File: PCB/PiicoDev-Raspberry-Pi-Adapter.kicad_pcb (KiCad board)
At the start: 2 copper layers, 22.1 x 51.6 mm, 12 parts, among them J1 Raspberry_Pi_2_3, J2 Conn_PiicoDev_socket, J3 Conn_PiicoDev_socket, J4 Conn_PiicoDev_socket, J5 Conn_PiicoDev_socket, J6 Prototyping Header

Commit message: Add Logo to silkscreen
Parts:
- added G***: LOGO, CoreElectronics_Artwork:CoreElectronics_logo_5mm_v2, F.Cu at (126.2, 77.3)

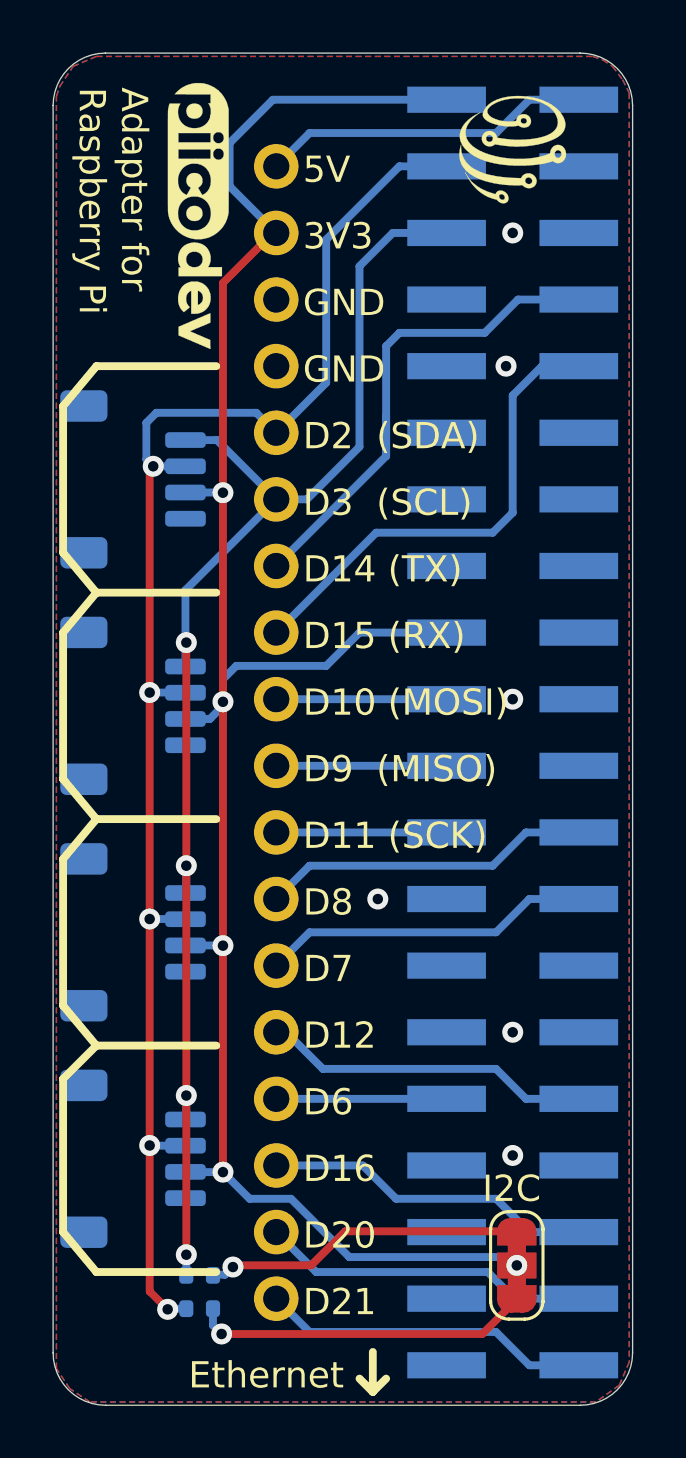
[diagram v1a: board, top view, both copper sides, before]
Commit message: Bump to v11 - update header footprint to include post-holes
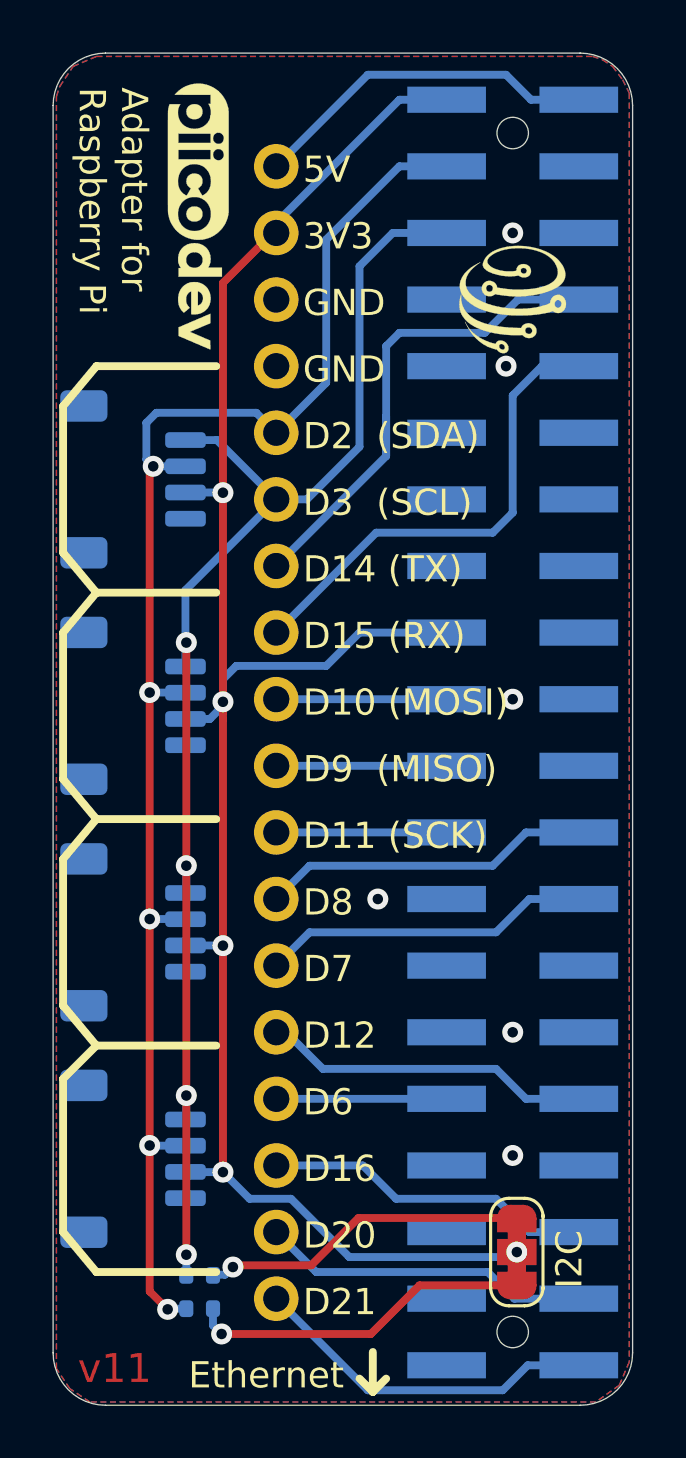
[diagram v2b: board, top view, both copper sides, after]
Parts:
- J1: footprint Connector_PinSocket_2.54mm:PinSocket_2x20_P2.54mm_Vertical_SMD -> CoreElectronics_Components:PinSocket_2x20_P2.54mm_Vertical_SMD_With_Post
- moved G*** 5.72 mm to (126.2, 83.1)
- moved JP1 0.51 mm to (126.4, 119.4)
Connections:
- J1 pad 11: (no net) -> Net-(J1-Pad11)
- J1 pad 12: (no net) -> Net-(J1-Pad12)
- J1 pad 13: (no net) -> Net-(J1-Pad13)
- J1 pad 15: (no net) -> Net-(J1-Pad15)
- J1 pad 16: (no net) -> Net-(J1-Pad16)
- J1 pad 18: (no net) -> Net-(J1-Pad18)
- J1 pad 22: (no net) -> Net-(J1-Pad22)
- J1 pad 27: (no net) -> Net-(J1-Pad27)
- J1 pad 28: (no net) -> Net-(J1-Pad28)
- J1 pad 29: (no net) -> Net-(J1-Pad29)
- J1 pad 33: (no net) -> Net-(J1-Pad33)
- J1 pad 34: GND -> Net-(J1-Pad34)
- J1 pad 35: (no net) -> Net-(J1-Pad35)
- J1 pad 37: (no net) -> Net-(J1-Pad37)
- J1 pad 39: GND -> Net-(J1-Pad39)
- J1 pad 4: (no net) -> Net-(J1-Pad4)
- J1 pad 7: (no net) -> Net-(J1-Pad7)
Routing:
- net +3V3: track 78.7 -> 74.4 mm
- net /D21: track 12.6 -> 13.4 mm
- net +5V: track 12.6 -> 13.4 mm
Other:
- board text added: "v11"

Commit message: Add 120R to SCL & SDA.  Improve silk screen.
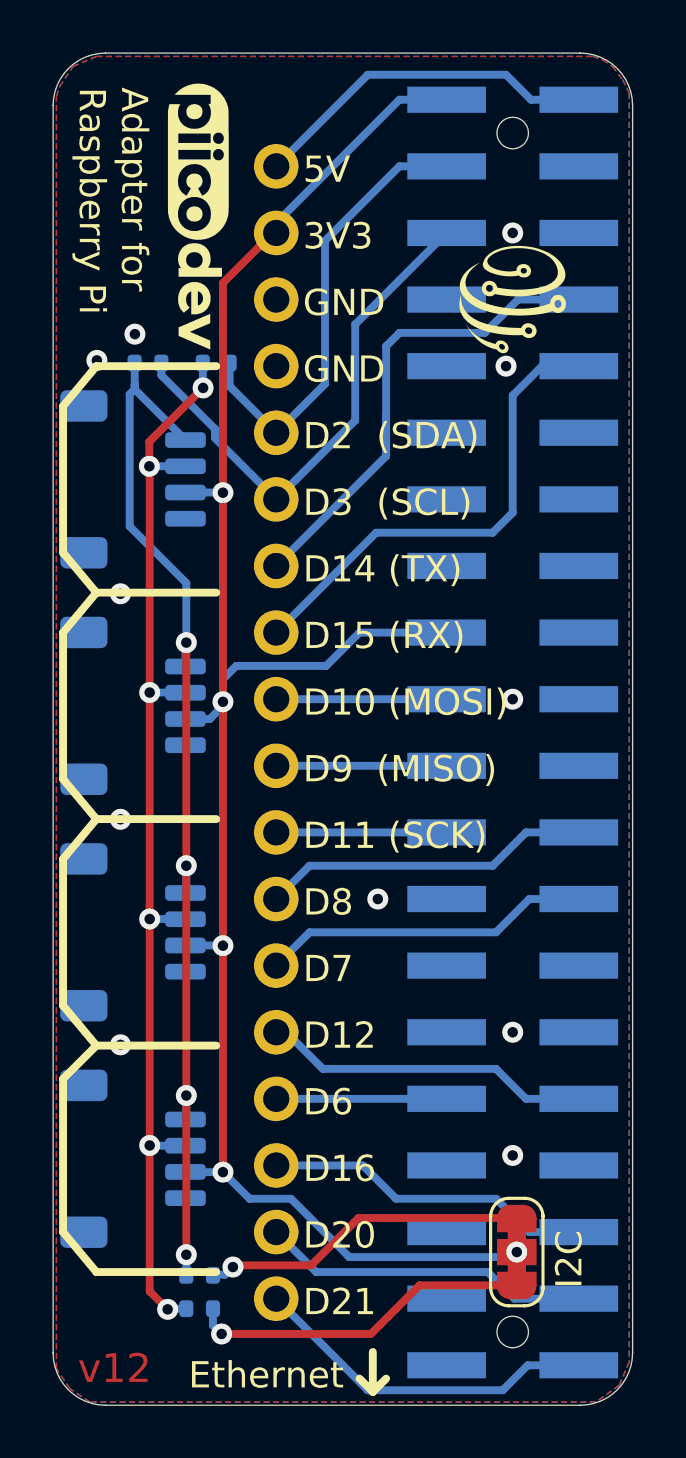
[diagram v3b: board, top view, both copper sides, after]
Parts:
- added R3: 120R, Resistor_SMD:R_0402_1005Metric, B.Cu at (114.9, 85.5)
- added R4: 120R, Resistor_SMD:R_0402_1005Metric, B.Cu at (112.3, 85.5)
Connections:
- J2 pad 3: /SDA -> /SDA_R
- J2 pad 4: /SCL -> /SCL_R
- J3 pad 3: /SDA -> /SDA_R
- J3 pad 4: /SCL -> /SCL_R
- J4 pad 3: /SDA -> /SDA_R
- J4 pad 4: /SCL -> /SCL_R
- J5 pad 1: GND -> Net-(J5-Pad1)
- J5 pad 3: /SDA -> /SDA_R
- J5 pad 4: /SCL -> /SCL_R
- R1 pad 2: /SDA -> /SDA_R
- R2 pad 2: /SCL -> /SCL_R
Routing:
- net /SDA_R: track 0.00 -> 43.7 mm, vias 0 -> 6
- net /SDA: track 59.6 -> 17.3 mm, vias 5 -> 0
- net /SCL_R: track 0.00 -> 41.6 mm, vias 0 -> 4
- net /SCL: track 53.1 -> 22.0 mm, vias 4 -> 0
- net GND: vias 6 -> 11
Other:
- board text added: "v12"
- board text removed: "v11"

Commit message: v13
Add Raspberry Pi connector pin numbers to silk screen
Update solder jumper with thinner cut trace
Fix PiicoDev connector ground connection
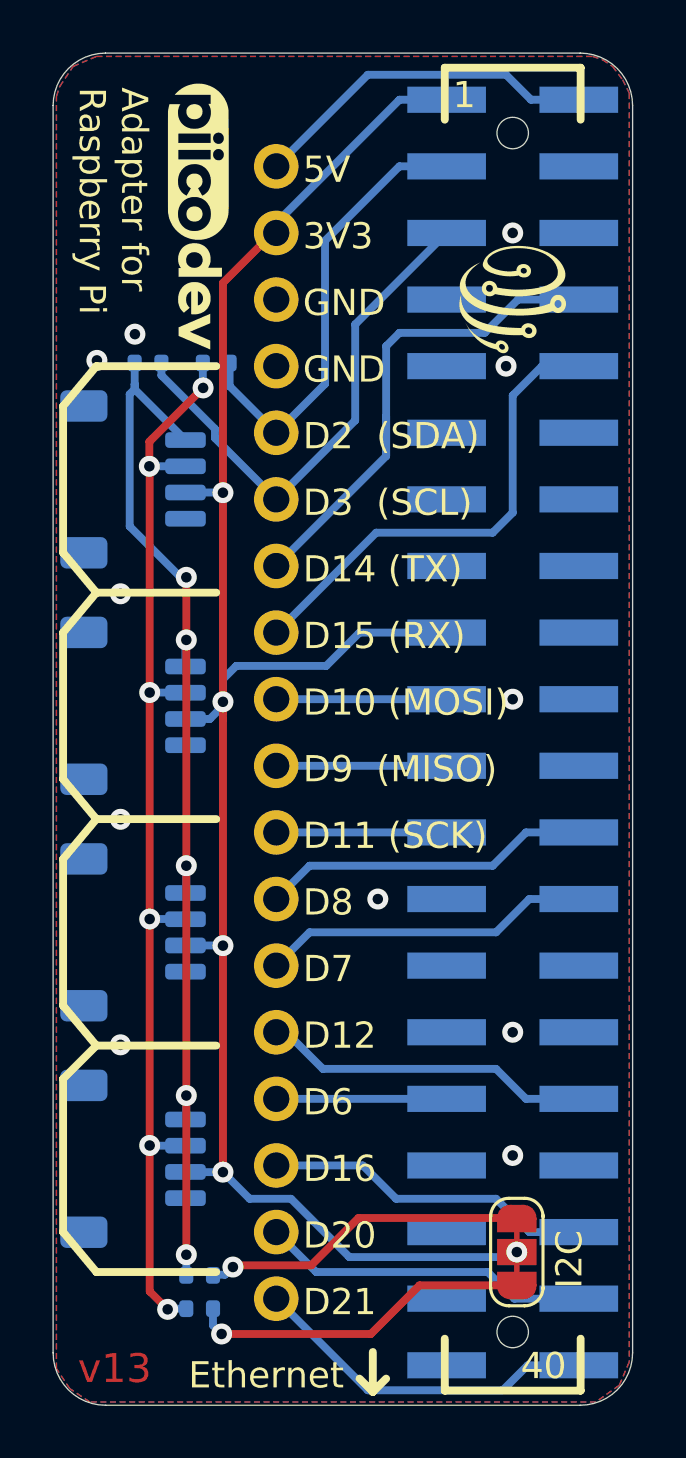
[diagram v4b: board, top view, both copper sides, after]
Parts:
- JP1: footprint CoreElectronics_Components:SolderJumper-3_P1.3mm_Closed_RoundedPad1.0x1.5mm -> CoreElectronics_Components:SolderJumper-3_P1.3mm_Closed_RoundedPad1.0x1.5mm_NumberLabels
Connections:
- J5 pad 1: Net-(J5-Pad1) -> GND
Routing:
- net /SCL_R: track 41.6 -> 41.7 mm, vias 4 -> 5
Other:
- board text added: "1"
- board text added: "40"
- board text added: "v13"
- board text removed: "v12"
